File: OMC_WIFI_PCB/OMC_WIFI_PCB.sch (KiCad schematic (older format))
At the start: 18 parts, among them J1 ESP32_Left, J10 Control_ACS712, J11 Control_ZMPT101B, J12 Power_Out_Load, J2 ESP32_Right, J3 Power_In, J4 Switch, J5 Pins_FT232R, J6 Line_Relay, J7 Control_Relay, J8 Line_ACS712, J9 Line_ZMPT101B, U1 LM741

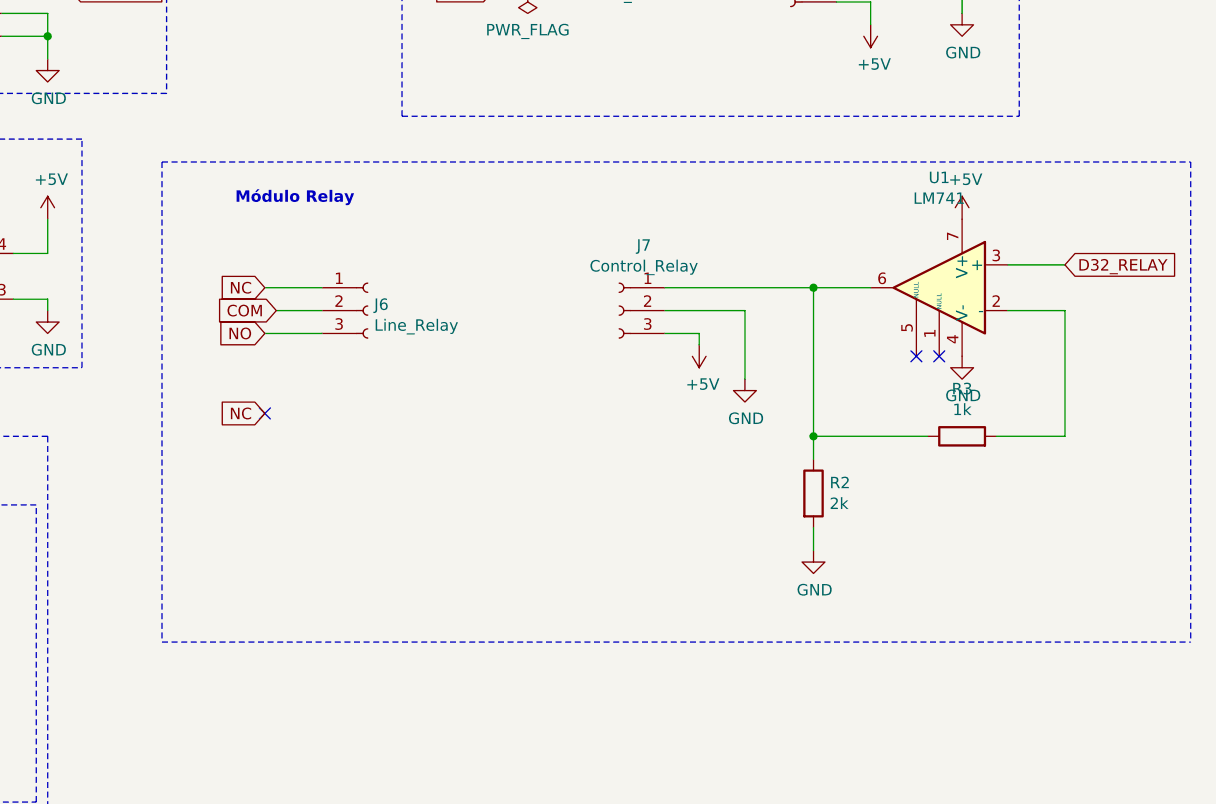
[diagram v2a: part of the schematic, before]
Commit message: Reestructuración PCB
> Cambio de posiciones
+ Anexar medidas
- Eliminar LM741
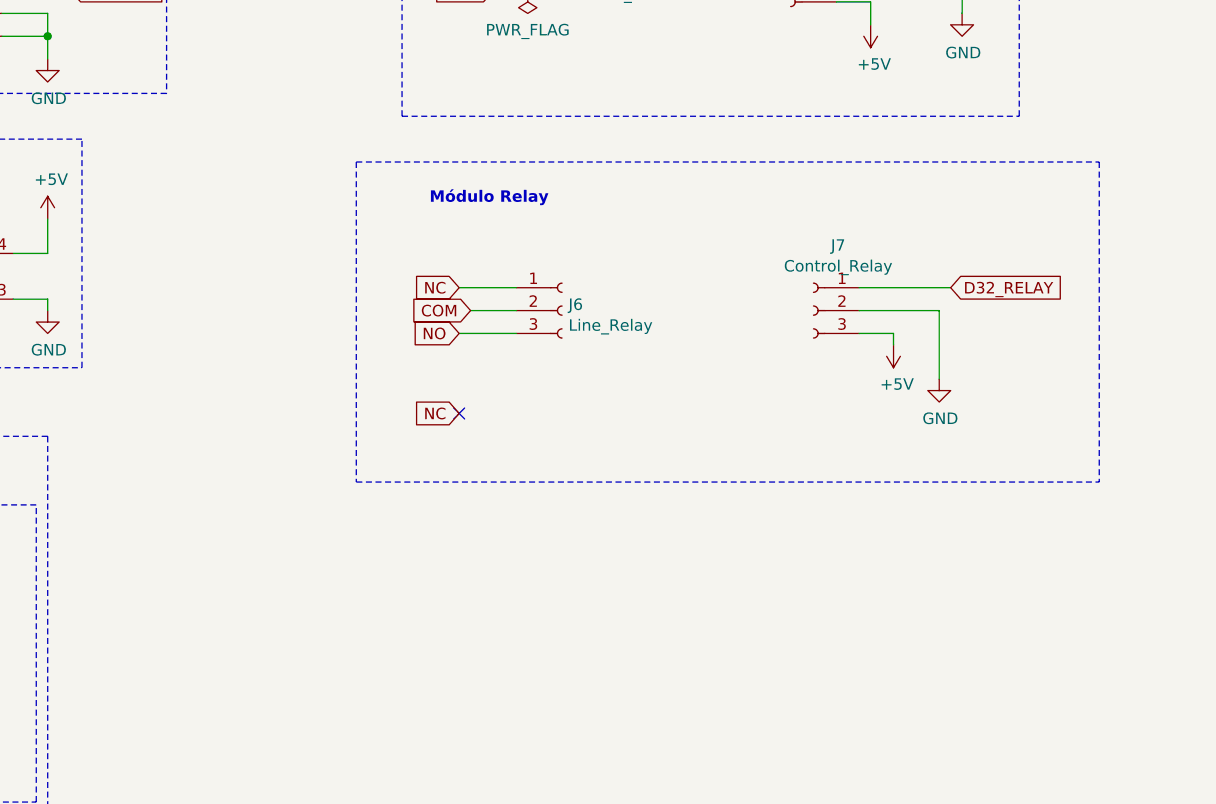
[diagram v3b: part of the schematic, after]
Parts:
- removed R2: 2k, Resistor_SMD:R_1812_4532Metric_Pad1.30x3.40mm_HandSolder, symbol Device:R
- removed R3: 1k, Resistor_SMD:R_2010_5025Metric_Pad1.40x2.65mm_HandSolder, symbol Device:R
- removed U1: LM741, Package_DIP:DIP-8_W10.16mm, symbol Amplifier_Operational:LM741
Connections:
- net D32_RELAY: now also J7.1 (Pin_1)
- no-connect marks 27 -> 25
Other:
- moved on the sheet: J6, J7
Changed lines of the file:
@@
 NoConn ~ 3050 7100
 NoConn ~ 3050 7200
-Wire Notes Line
-	6550 4150 11050 4150
-Wire Notes Line
-	6550 2050 6550 4150
-Wire Notes Line
-	11050 2050 11050 4150
-Connection ~ 9400 2600
-Wire Wire Line
-	8750 2600 9400 2600
-Wire Wire Line
-	10250 2500 10500 2500
-Wire Wire Line
-	10500 2700 10250 2700
-Wire Wire Line
-	10500 3250 10500 2700
-Wire Wire Line
-	10200 3250 10500 3250
-Connection ~ 9400 3250
-Wire Wire Line
-	9400 2600 9650 2600
-Wire Wire Line
-	9400 3250 9400 2600
-Wire Wire Line
-	9400 3650 9400 3750
-$Comp
-L power:GND #PWR0111
-U 1 1 6220F94A
-P 9400 3750
-F 0 "#PWR0111" H 9400 3500 50  0001 C CNN
-F 1 "GND" H 9405 3577 50  0000 C CNN
-F 2 "" H 9400 3750 50  0001 C CNN
-F 3 "" H 9400 3750 50  0001 C CNN
-	1    9400 3750
-	1    0    0    -1
-$EndComp
-Wire Wire Line
-	9400 3250 9400 3350
-Wire Wire Line
-	9900 3250 9400 3250
-$Comp
-L Device:R R2
-U 1 1 621C4D2D
-P 9400 3500
-F 0 "R2" H 9470 3546 50  0000 L CNN
-F 1 "2k" H 9470 3455 50  0000 L CNN
-F 2 "Resistor_SMD:R_1812_4532Metric_Pad1.30x3.40mm_HandSolder" V 9330 3500 50  0001 C CNN
-F 3 "~" H 9400 3500 50  0001 C CNN
-	1    9400 3500
-	1    0    0    -1
-$EndComp
-$Comp
-L Device:R R3
-U 1 1 621C38B5
-P 10050 3250
-F 0 "R3" V 10257 3250 50  0000 C CNN
-F 1 "1k" V 10166 3250 50  0000 C CNN
-F 2 "Resistor_SMD:R_2010_5025Metric_Pad1.40x2.65mm_HandSolder" V 9980 3250 50  0001 C CNN
-F 3 "~" H 10050 3250 50  0001 C CNN
-	1    10050 3250
-	0    -1   -1   0
-$EndComp
-$Comp
-L power:GND #PWR0112
-U 1 1 621BD23A
-P 10050 2900
-F 0 "#PWR0112" H 10050 2650 50  0001 C CNN
-F 1 "GND" H 10055 2727 50  0000 C CNN
-F 2 "" H 10050 2900 50  0001 C CNN
-F 3 "" H 10050 2900 50  0001 C CNN
-	1    10050 2900
-	1    0    0    -1
-$EndComp
-$Comp
-L power:+5V #PWR0113
-U 1 1 621B69B1
-P 10050 2300
-F 0 "#PWR0113" H 10050 2150 50  0001 C CNN
-F 1 "+5V" H 10065 2473 50  0000 C CNN
-F 2 "" H 10050 2300 50  0001 C CNN
-F 3 "" H 10050 2300 50  0001 C CNN
-	1    10050 2300
-	1    0    0    -1
-$EndComp
-$Comp
-L Amplifier_Operational:LM741 U1
-U 1 1 621A7382
-P 9950 2600
-F 0 "U1" H 9950 3081 50  0000 C CNN
-F 1 "LM741" H 9950 2990 50  0000 C CNN
-F 2 "Package_DIP:DIP-8_W10.16mm" H 10000 2650 50  0001 C CNN
-F 3 "http://www.ti.com/lit/ds/symlink/lm741.pdf" H 10100 2750 50  0001 C CNN
-	1    9950 2600
-	-1   0    0    -1
-$EndComp
-Wire Wire Line
-	7000 2800 7250 2800
-Wire Wire Line
-	7050 2700 7250 2700
-Wire Wire Line
-	7000 2600 7250 2600
-Wire Wire Line
-	8900 2800 8900 2850
-Wire Wire Line
-	8750 2800 8900 2800
-Wire Wire Line
-	9100 2700 9100 3000
-Wire Wire Line
-	8750 2700 9100 2700
+Wire Wire Line
+	7850 2800 8100 2800
+Wire Wire Line
+	7900 2700 8100 2700
+Wire Wire Line
+	7850 2600 8100 2600
+Wire Wire Line
+	9750 2800 9750 2850
+Wire Wire Line
+	9600 2800 9750 2800
+Wire Wire Line
+	9950 2700 9950 3000
+Wire Wire Line
+	9600 2700 9950 2700
 $Comp
 L power:+5V #PWR0114
 U 1 1 623FD4D5
-P 8900 2850
-F 0 "#PWR0114" H 8900 2700 50  0001 C CNN
-F 1 "+5V" H 8915 3023 50  0000 C CNN
-F 2 "" H 8900 2850 50  0001 C CNN
-F 3 "" H 8900 2850 50  0001 C CNN
-	1    8900 2850
+P 9750 2850
+F 0 "#PWR0114" H 9750 2700 50  0001 C CNN
+F 1 "+5V" H 9765 3023 50  0000 C CNN
+F 2 "" H 9750 2850 50  0001 C CNN
+F 3 "" H 9750 2850 50  0001 C CNN
+	1    9750 2850
 	1    0    0    1
 $EndComp
@@
 L power:GND #PWR0115
 U 1 1 623FCDC3
-P 9100 3000
-F 0 "#PWR0115" H 9100 2750 50  0001 C CNN
-F 1 "GND" H 9105 2827 50  0000 C CNN
-F 2 "" H 9100 3000 50  0001 C CNN
-F 3 "" H 9100 3000 50  0001 C CNN
-	1    9100 3000
-	1    0    0    -1
-$EndComp
-Text GLabel 10500 2500 2    50   Input ~ 0
+P 9950 3000
+F 0 "#PWR0115" H 9950 2750 50  0001 C CNN
+F 1 "GND" H 9955 2827 50  0000 C CNN
+F 2 "" H 9950 3000 50  0001 C CNN
+F 3 "" H 9950 3000 50  0001 C CNN
+	1    9950 3000
+	1    0    0    -1
+$EndComp
+Text GLabel 10000 2600 2    50   Input ~ 0
 D32_RELAY
-Text GLabel 7050 2700 0    50   Input ~ 0
+Text GLabel 7900 2700 0    50   Input ~ 0
 COM
-Text GLabel 7000 2600 0    50   Input ~ 0
+Text GLabel 7850 2600 0    50   Input ~ 0
 NC
-Text GLabel 7000 2800 0    50   Input ~ 0
+Text GLabel 7850 2800 0    50   Input ~ 0
 NO
 $Comp
 L Connector:Conn_01x03_Female J7
 U 1 1 623E700B
-P 8550 2700
-F 0 "J7" H 8442 2985 50  0000 C CNN
-F 1 "Control_Relay" H 8442 2894 50  0000 C CNN
-F 2 "Connector_Wire:SolderWire-0.75sqmm_1x03_P4.8mm_D1.25mm_OD2.3mm" H 8550 2700 50  0001 C CNN
-F 3 "~" H 8550 2700 50  0001 C CNN
-	1    8550 2700
+P 9400 2700
+F 0 "J7" H 9292 2985 50  0000 C CNN
+F 1 "Control_Relay" H 9292 2894 50  0000 C CNN
+F 2 "Connector_Wire:SolderWire-0.75sqmm_1x03_P4.8mm_D1.25mm_OD2.3mm" H 9400 2700 50  0001 C CNN
+F 3 "~" H 9400 2700 50  0001 C CNN
+	1    9400 2700
 	-1   0    0    -1
 $EndComp
@@
 L Connector:Conn_01x03_Female J6
 U 1 1 623E5D69
-P 7450 2700
-F 0 "J6" H 7478 2726 50  0000 L CNN
-F 1 "Line_Relay" H 7478 2635 50  0000 L CNN
-F 2 "Connector_Wire:SolderWire-0.75sqmm_1x03_P4.8mm_D1.25mm_OD2.3mm" H 7450 2700 50  0001 C CNN
-F 3 "~" H 7450 2700 50  0001 C CNN
-	1    7450 2700
-	1    0    0    -1
-$EndComp
-Text Notes 6870 2240 0    50   ~ 10
+P 8300 2700
+F 0 "J6" H 8328 2726 50  0000 L CNN
+F 1 "Line_Relay" H 8328 2635 50  0000 L CNN
+F 2 "Connector_Wire:SolderWire-0.75sqmm_1x03_P4.8mm_D1.25mm_OD2.3mm" H 8300 2700 50  0001 C CNN
+F 3 "~" H 8300 2700 50  0001 C CNN
+	1    8300 2700
+	1    0    0    -1
+$EndComp
+Text Notes 7720 2240 0    50   ~ 10
 Módulo Relay\n
 $Comp
@@
 Wire Notes Line
 	4350 5050 4350 5950
-NoConn ~ 9850 2900
-NoConn ~ 9950 2900
-Text GLabel 7000 3150 0    50   Input ~ 0
+Text GLabel 7850 3150 0    50   Input ~ 0
 NC
-NoConn ~ 7000 3150
+NoConn ~ 7850 3150
 $Comp
 L Connector:Screw_Terminal_01x03 J12
@@
 Wire Notes Line
 	6200 1950 4350 1950
-Wire Notes Line
-	6550 2050 11050 2050
 NoConn ~ 5550 4700
 NoConn ~ 5550 4600
@@
 	1    0    0    -1
 $EndComp
+Wire Wire Line
+	9600 2600 10000 2600
+Wire Notes Line
+	7400 2050 10650 2050
+Wire Notes Line
+	10650 2050 10650 3450
+Wire Notes Line
+	7400 2050 7400 3450
+Wire Notes Line
+	7400 3450 10650 3450
 $EndSCHEMATC

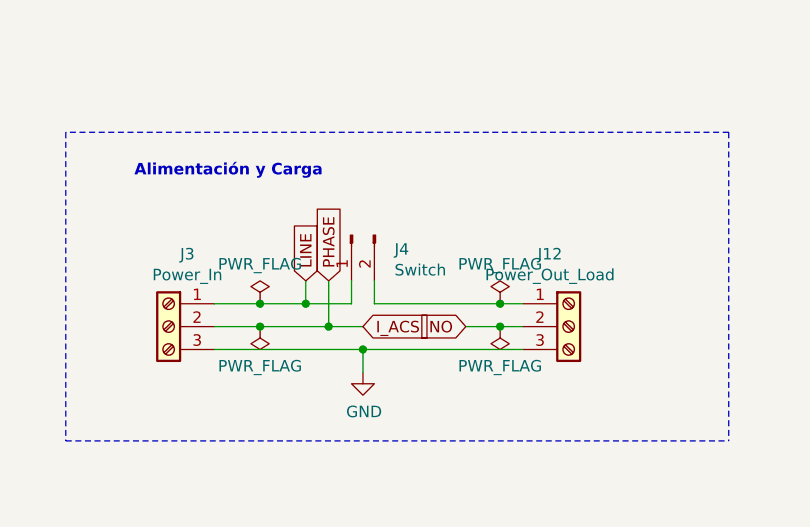
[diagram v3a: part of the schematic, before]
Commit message: Actualización PCB
+ Medidas de ZMPT101B
+ Medidas Módulo Relay
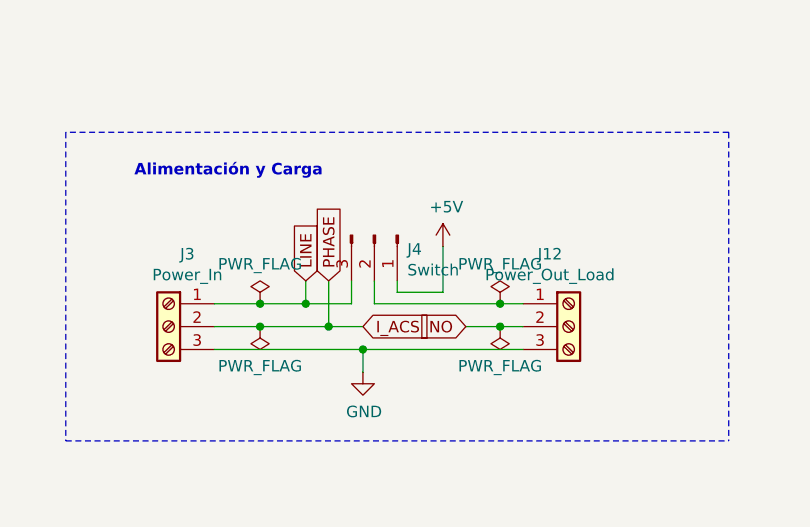
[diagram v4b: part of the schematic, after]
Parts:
- removed J4: Switch, Connector_Wire:SolderWire-0.75sqmm_1x02_P7mm_D1.25mm_OD3.5mm, symbol Connector:Conn_01x02_Male
- added J4: Switch, Connector_Wire:SolderWire-0.75sqmm_1x03_P4.8mm_D1.25mm_OD2.3mm, symbol Connector:Conn_01x03_Male
- J6, J7: footprint Connector_Wire:SolderWire-0.75sqmm_1x03_P4.8mm_D1.25mm_OD2.3mm -> TerminalBlock:TerminalBlock_bornier-3_P5.08mm
- J8, J9: footprint Connector_Wire:SolderWire-0.75sqmm_1x02_P4.8mm_D1.25mm_OD2.3mm -> TerminalBlock:TerminalBlock_bornier-2_P5.08mm
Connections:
- net +5V: now also J4.1 (Pin_1)
- net LINE: now also J4.3 (Pin_3)
- net at J12.1 (Pin_1): now also J4.2 (Pin_2)
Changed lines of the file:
@@
 	950  5450 1850 5450
-$Comp
-L Connector:Conn_01x02_Male J4
-U 1 1 62292DE9
-P 2150 1650
-F 0 "J4" V 2212 1462 50  0000 R CNN
-F 1 "Switch" V 2303 1462 50  0000 R CNN
-F 2 "Connector_Wire:SolderWire-0.75sqmm_1x02_P7mm_D1.25mm_OD3.5mm" H 2150 1650 50  0001 C CNN
-F 3 "~" H 2150 1650 50  0001 C CNN
-	1    2150 1650
-	0    -1   1    0
-$EndComp
 $Comp
 L Converter_ACDC:HLK-PM01 PS1
@@
 F 0 "J7" H 9292 2985 50  0000 C CNN
 F 1 "Control_Relay" H 9292 2894 50  0000 C CNN
-F 2 "Connector_Wire:SolderWire-0.75sqmm_1x03_P4.8mm_D1.25mm_OD2.3mm" H 9400 2700 50  0001 C CNN
+F 2 "TerminalBlock:TerminalBlock_bornier-3_P5.08mm" H 9400 2700 50  0001 C CNN
 F 3 "~" H 9400 2700 50  0001 C CNN
 	1    9400 2700
@@
 F 0 "J6" H 8328 2726 50  0000 L CNN
 F 1 "Line_Relay" H 8328 2635 50  0000 L CNN
-F 2 "Connector_Wire:SolderWire-0.75sqmm_1x03_P4.8mm_D1.25mm_OD2.3mm" H 8300 2700 50  0001 C CNN
+F 2 "TerminalBlock:TerminalBlock_bornier-3_P5.08mm" H 8300 2700 50  0001 C CNN
 F 3 "~" H 8300 2700 50  0001 C CNN
 	1    8300 2700
@@
 F 0 "J8" H 8428 1176 50  0000 L CNN
 F 1 "Line_ACS712" H 8428 1085 50  0000 L CNN
-F 2 "Connector_Wire:SolderWire-0.75sqmm_1x02_P4.8mm_D1.25mm_OD2.3mm" H 8400 1200 50  0001 C CNN
+F 2 "TerminalBlock:TerminalBlock_bornier-2_P5.08mm" H 8400 1200 50  0001 C CNN
 F 3 "~" H 8400 1200 50  0001 C CNN
 	1    8400 1200
@@
 F 0 "J9" H 5178 1276 50  0000 L CNN
 F 1 "Line_ZMPT101B" H 5178 1185 50  0000 L CNN
-F 2 "Connector_Wire:SolderWire-0.75sqmm_1x02_P4.8mm_D1.25mm_OD2.3mm" H 5150 1300 50  0001 C CNN
+F 2 "TerminalBlock:TerminalBlock_bornier-2_P5.08mm" H 5150 1300 50  0001 C CNN
 F 3 "~" H 5150 1300 50  0001 C CNN
 	1    5150 1300
@@
 Wire Notes Line
 	7400 3450 10650 3450
+$Comp
+L Connector:Conn_01x03_Male J4
+U 1 1 6216C21C
+P 2250 1650
+F 0 "J4" V 2312 1794 50  0000 L CNN
+F 1 "Switch" V 2403 1794 50  0000 L CNN
+F 2 "Connector_Wire:SolderWire-0.75sqmm_1x03_P4.8mm_D1.25mm_OD2.3mm" H 2250 1650 50  0001 C CNN
+F 3 "~" H 2250 1650 50  0001 C CNN
+	1    2250 1650
+	0    1    1    0
+$EndComp
+$Comp
+L power:+5V #PWR0111
+U 1 1 62178CC2
+P 2550 1700
+F 0 "#PWR0111" H 2550 1550 50  0001 C CNN
+F 1 "+5V" H 2565 1873 50  0000 C CNN
+F 2 "" H 2550 1700 50  0001 C CNN
+F 3 "" H 2550 1700 50  0001 C CNN
+	1    2550 1700
+	1    0    0    -1
+$EndComp
+Wire Wire Line
+	2350 1850 2350 1900
+Wire Wire Line
+	2350 1900 2550 1900
+Wire Wire Line
+	2550 1900 2550 1700
 $EndSCHEMATC

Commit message: Actualización PCB
+ Medidas ACS712
- Conexión 5V al switch
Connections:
- net +5V: no longer J4.1 (Pin_1)
- no-connect marks 25 -> 26
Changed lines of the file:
@@
 	0    1    1    0
 $EndComp
-$Comp
-L power:+5V #PWR0111
-U 1 1 62178CC2
-P 2550 1700
-F 0 "#PWR0111" H 2550 1550 50  0001 C CNN
-F 1 "+5V" H 2565 1873 50  0000 C CNN
-F 2 "" H 2550 1700 50  0001 C CNN
-F 3 "" H 2550 1700 50  0001 C CNN
-	1    2550 1700
-	1    0    0    -1
-$EndComp
-Wire Wire Line
-	2350 1850 2350 1900
-Wire Wire Line
-	2350 1900 2550 1900
-Wire Wire Line
-	2550 1900 2550 1700
+NoConn ~ 2350 1850
 $EndSCHEMATC
